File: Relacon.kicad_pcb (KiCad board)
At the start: 2 copper layers, 85.7 x 54 mm, 53 parts, among them J1 USB_B, J2 Conn_02x10_Odd_Even, J3 Conn_01x16, U1 STM32F042K6Tx, U10 AQY212GS, U11 AQY212GS, U2 AMS1117-3.3, U3 ULN2803A, U4 AQY212GS, U5 AQY212GS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

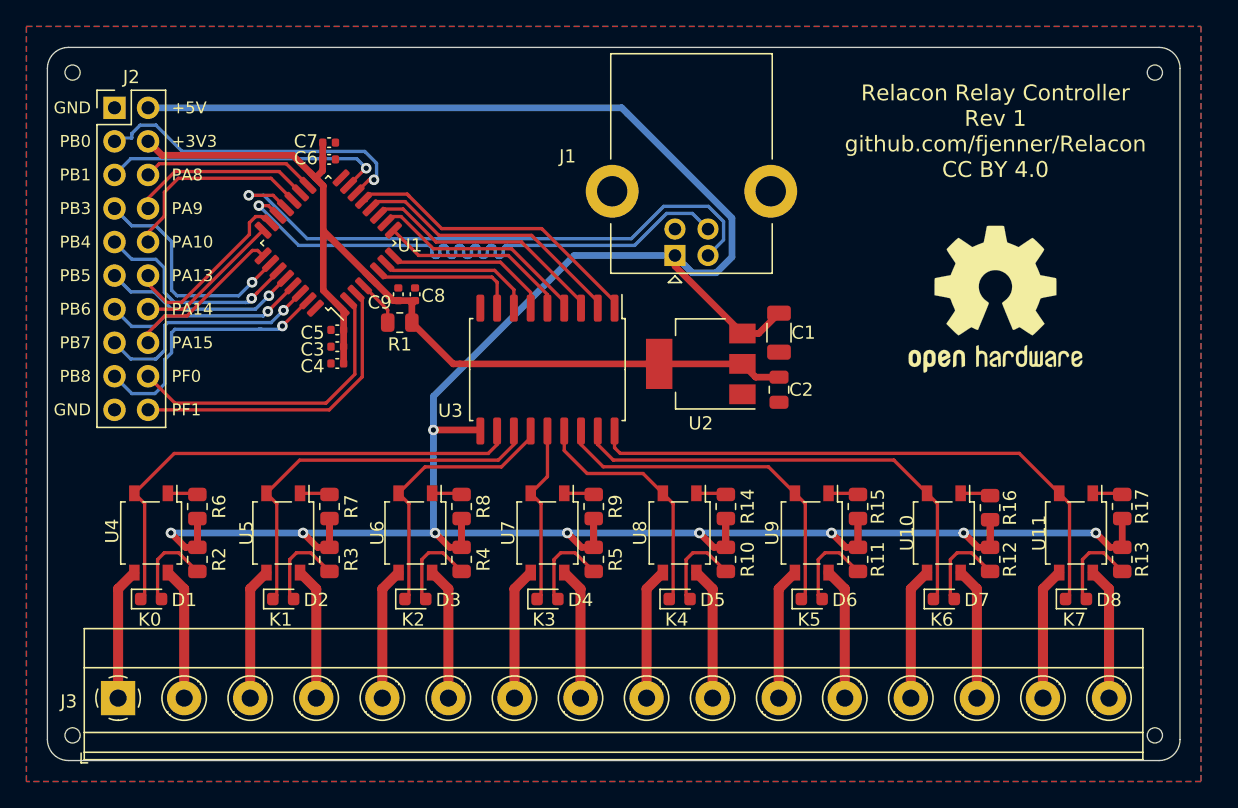
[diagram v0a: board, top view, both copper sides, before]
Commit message: Updated URL on silk screen
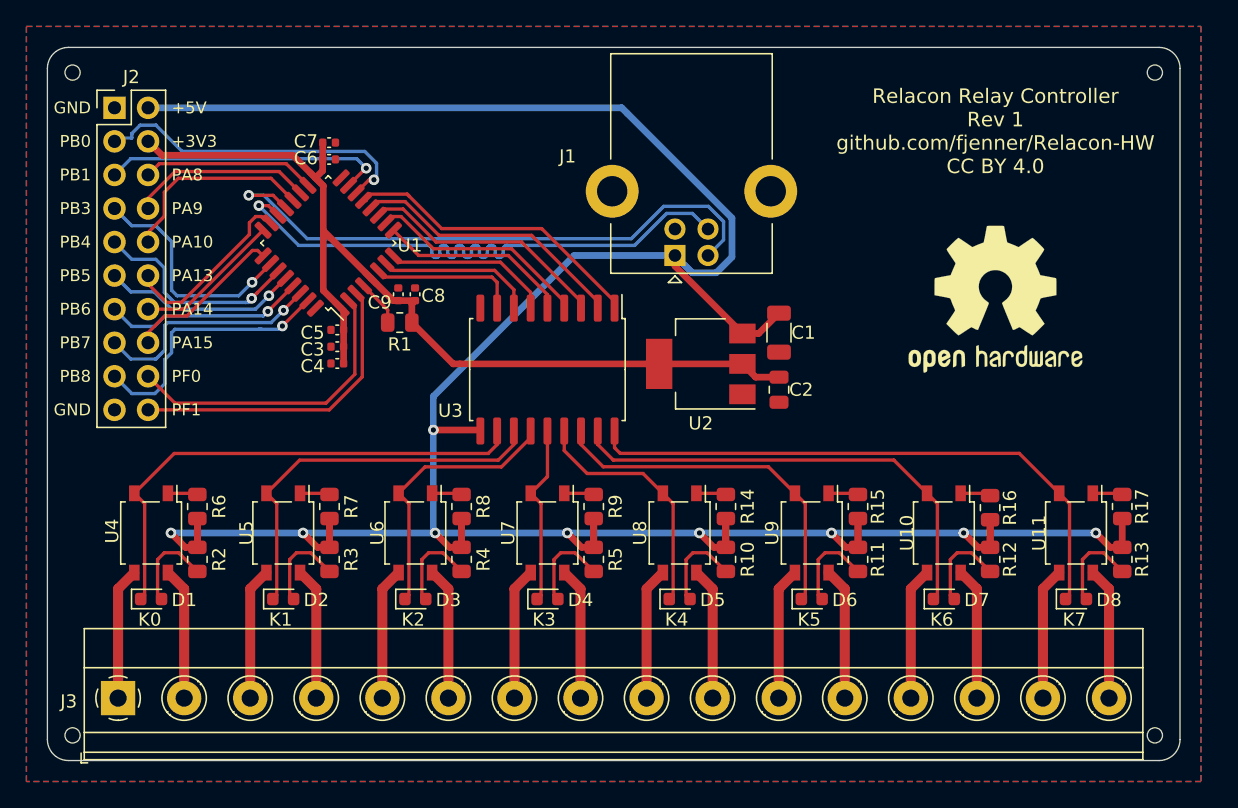
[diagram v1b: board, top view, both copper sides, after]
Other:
- board text added: "Relacon Relay Controller Rev 1 github.com/fjenner/Relacon-HW CC BY 4.0"
- board text removed: "Relacon Relay Controller Rev 1 github.com/fjenner/Relacon CC BY 4.0"
